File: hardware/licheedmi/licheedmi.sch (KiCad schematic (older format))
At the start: 17 parts

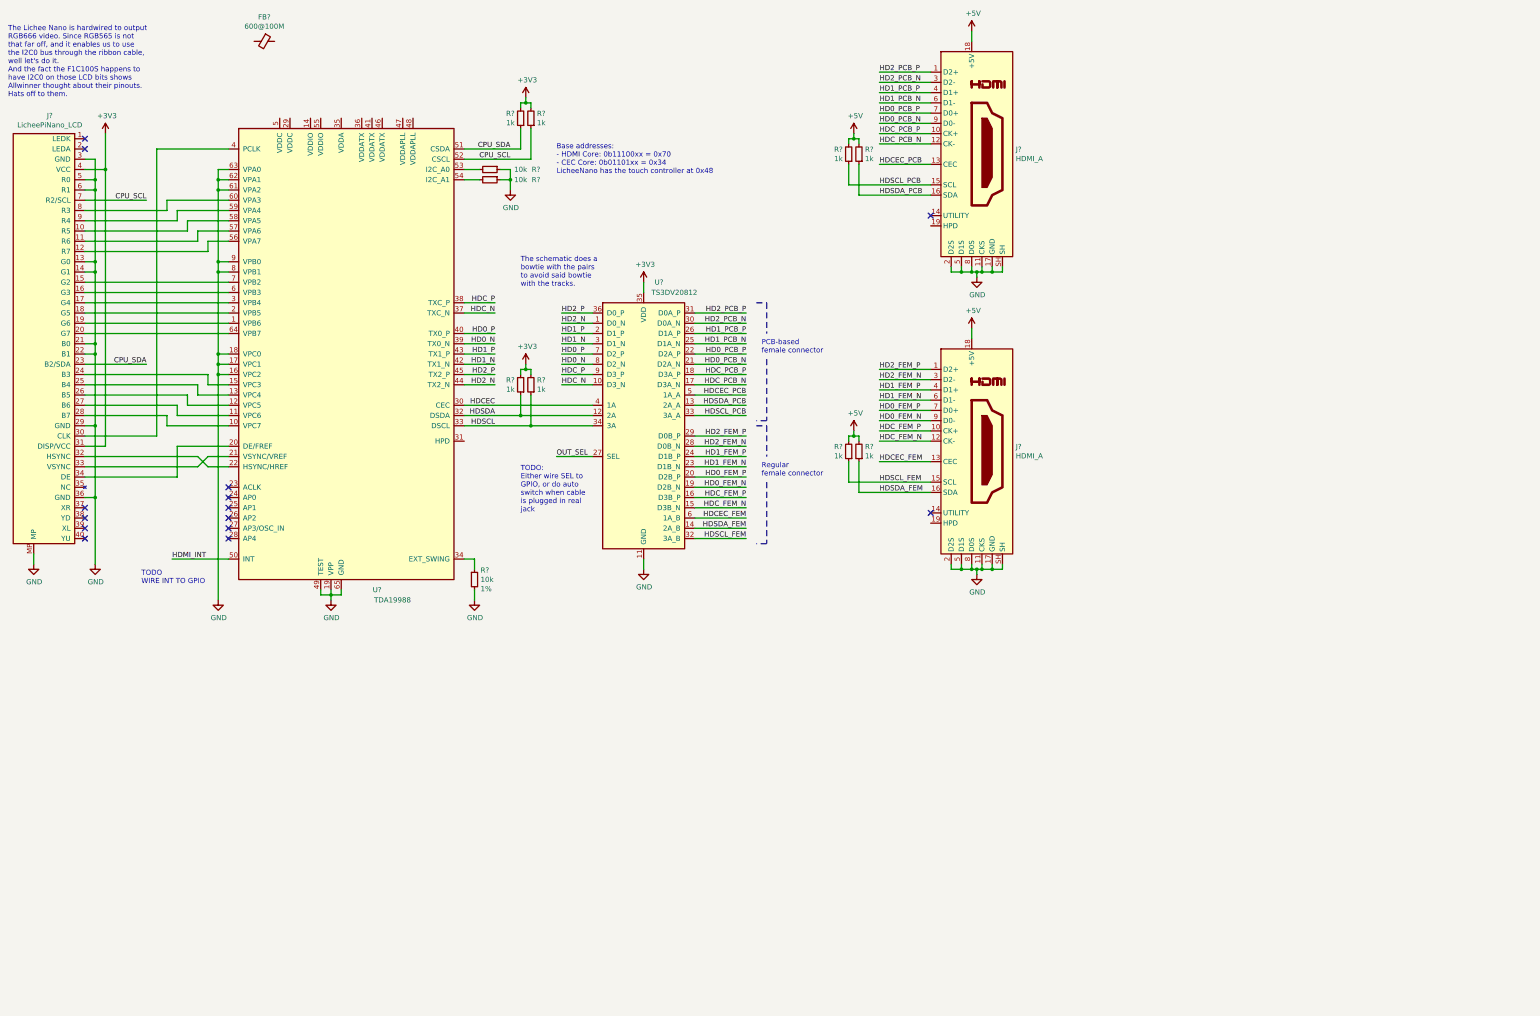
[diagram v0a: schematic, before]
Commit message: sch: Add HDMI 1.8V PSU
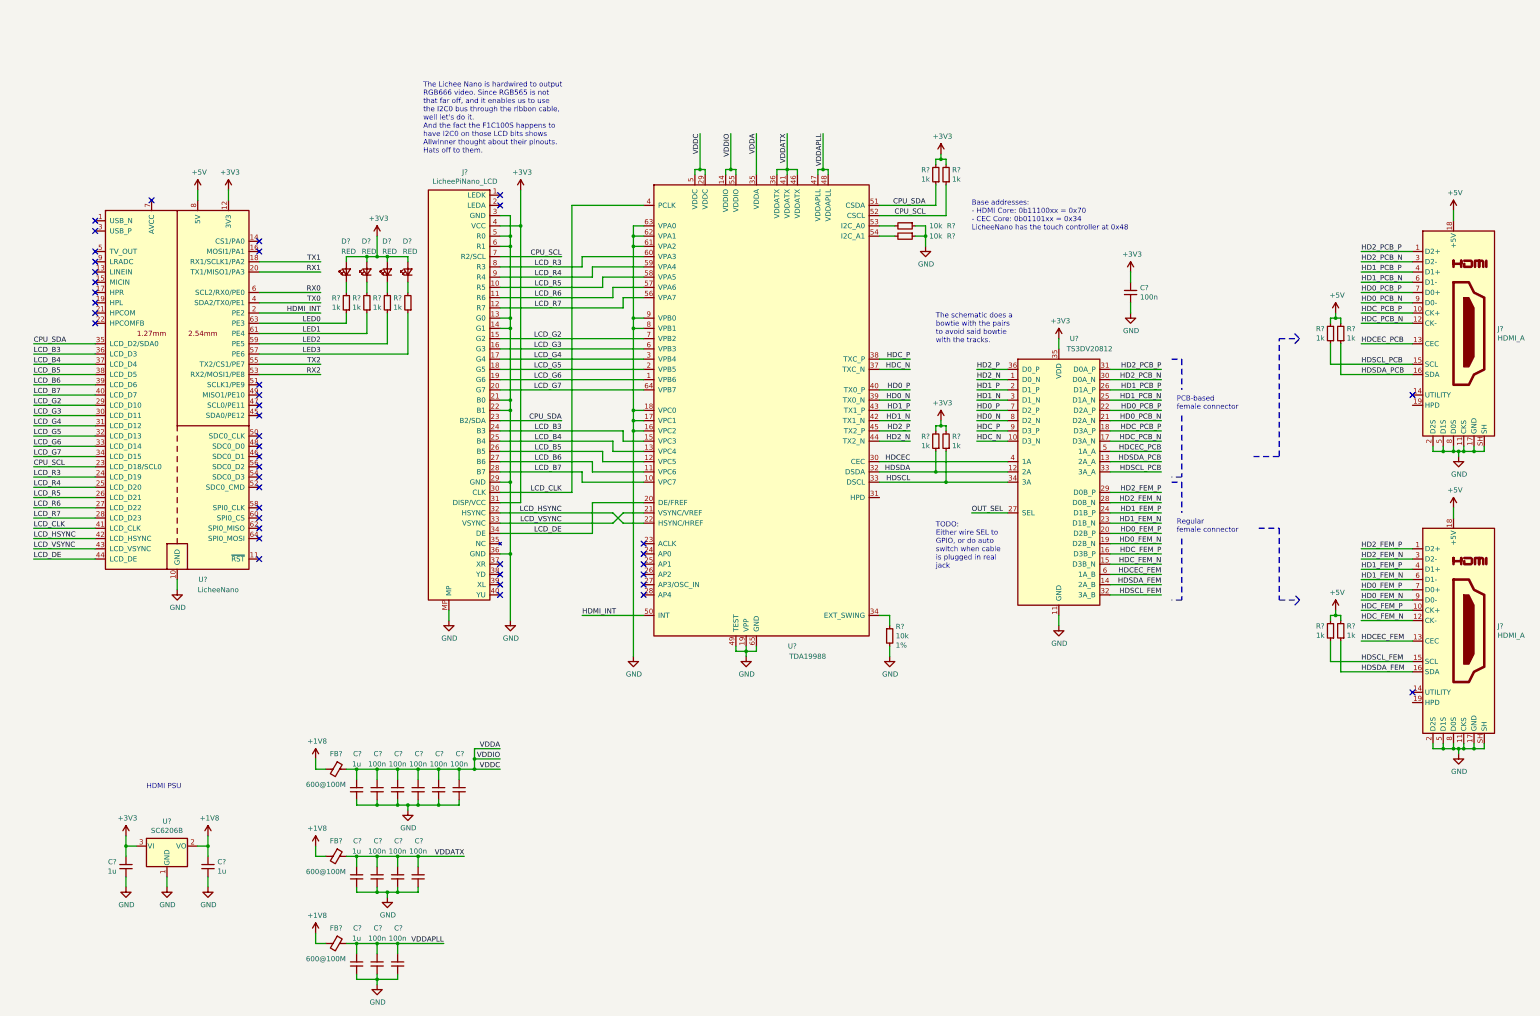
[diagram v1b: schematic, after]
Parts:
- added C? (x5): 1u, Capacitor_SMD:C_0603_1608Metric, symbol Device:C_Small
- added C? (x11): 100n, Capacitor_SMD:C_0603_1608Metric, symbol Device:C_Small
- added D? (x4): RED, symbol Device:LED_Small
- added FB? (x2): 600@100M, Inductor_SMD:L_0603_1608Metric, symbol Device:Ferrite_Bead_Small
- added R? (x4): 1k, Resistor_SMD:R_0603_1608Metric, symbol Device:R_Small
- added U?: LicheeNano, hdmizness:LicheeNano, symbol hdmizness:LicheeNano
- added U?: SC6206B, Package_TO_SOT_SMD:SOT-23, symbol hdmizness:SC6206B
- FB?: footprint (none) -> Inductor_SMD:L_0603_1608Metric
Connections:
- net +3V3: now also C?.1, C?.1, D?.2 (A), D?.2 (A), D?.2 (A), D?.2 (A), U?.12 (3V3), U?.3 (VI)
- net +5V: now also U?.8 (5V)
- net CPU_SCL: now also U?.23 (LCD_D18/SCL0)
- net CPU_SDA: now also U?.35 (LCD_D2/SDA0)
- net GND: now also C?.2, C?.2, C?.2, C?.2, C?.2, C?.2, C?.2, C?.2, C?.2, C?.2, C?.2, C?.2, C?.2, C?.2, C?.2, C?.2, U?.1 (GND), U?.10 (GND)
- net HDMI_INT: now also U?.2 (PE2)
- net LCD_G6: now reaches J?.19 (G6), U?.1 (VPB6)
- net LCD_G6: now also U?.33 (LCD_D14)
- net LCD_B7: now reaches J?.28 (B7), U?.10 (VPC7)
- net LCD_B7: now also U?.40 (LCD_D7)
- net LCD_B6: now reaches J?.27 (B6), U?.11 (VPC6)
- net LCD_B6: now also U?.39 (LCD_D6)
- net LCD_B5: now reaches J?.26 (B5), U?.12 (VPC5)
- net LCD_B5: now also U?.38 (LCD_D5)
- net LCD_B4: now reaches J?.25 (B4), U?.13 (VPC4)
- net LCD_B4: now also U?.37 (LCD_D4)
- net VDDA: now reaches U?.14 (VDDIO)
- net VDDA: now also U?.29 (VDDC), U?.35 (VDDA), U?.5 (VDDC), U?.55 (VDDIO), C?.1, C?.1, C?.1, C?.1, C?.1, C?.1, FB?.1
- net LCD_B3: now reaches J?.24 (B3), U?.15 (VPC3)
- net LCD_B3: now also U?.36 (LCD_D3)
- net LCD_G5: now reaches J?.18 (G5), U?.2 (VPB5)
- net LCD_G5: now also U?.32 (LCD_D13)
- net LCD_DE: now reaches J?.34 (DE), U?.20 (DE/FREF)
- net LCD_DE: now also U?.44 (LCD_DE)
- net LCD_VSYNC: now reaches J?.33 (VSYNC), U?.21 (VSYNC/VREF)
- net LCD_VSYNC: now also U?.43 (LCD_VSYNC)
- net LCD_HSYNC: now reaches J?.32 (HSYNC), U?.22 (HSYNC/HREF)
- net LCD_HSYNC: now also U?.42 (LCD_HSYNC)
- net LCD_G4: now reaches J?.17 (G4), U?.3 (VPB4)
- net LCD_G4: now also U?.31 (LCD_D12)
- net VDDATX: now reaches U?.36 (VDDATX)
- net VDDATX: now also FB?.1, U?.41 (VDDATX), U?.46 (VDDATX), C?.1, C?.1, C?.1, C?.1
- net LCD_CLK: now reaches J?.30 (CLK), U?.4 (PCLK)
- net LCD_CLK: now also U?.41 (LCD_CLK)
- net VDDAPLL: now reaches U?.47 (VDDAPLL)
- net VDDAPLL: now also U?.48 (VDDAPLL), C?.1, C?.1, C?.1, FB?.1
- net LCD_R7: now reaches J?.12 (R7), U?.56 (VPA7)
- net LCD_R7: now also U?.28 (LCD_D23)
- net LCD_R6: now reaches J?.11 (R6), U?.57 (VPA6)
- net LCD_R6: now also U?.27 (LCD_D22)
- net LCD_R5: now reaches J?.10 (R5), U?.58 (VPA5)
- net LCD_R5: now also U?.26 (LCD_D21)
- net LCD_R4: now reaches J?.9 (R4), U?.59 (VPA4)
- net LCD_R4: now also U?.25 (LCD_D20)
- net LCD_G3: now reaches J?.16 (G3), U?.6 (VPB3)
- net LCD_G3: now also U?.30 (LCD_D11)
- net LCD_R3: now reaches J?.8 (R3), U?.60 (VPA3)
- net LCD_R3: now also U?.24 (LCD_D19)
- net LCD_G7: now reaches J?.20 (G7), U?.64 (VPB7)
- net LCD_G7: now also U?.34 (LCD_D15)
- net LCD_G2: now reaches J?.15 (G2), U?.7 (VPB2)
- net LCD_G2: now also U?.29 (LCD_D10)
- net +1V8: now reaches FB?.2
- net +1V8: now also C?.1, FB?.2, FB?.2, U?.2 (VO)
- new net: D?.1 (K), R?.2 (x4)
- new net LED0: R?.1, U?.63 (PE3)
- new net LED1: R?.1, U?.61 (PE4)
- new net LED2: R?.1, U?.59 (PE5)
- new net LED3: R?.1, U?.57 (PE6)
- new net RX0: U?.6 (SCL2/RX0/PE0)
- new net RX1: U?.20 (TX1/MISO1/PA3)
- new net RX2: U?.53 (RX2/MOSI1/PE8)
- new net TX0: U?.4 (SDA2/TX0/PE1)
- new net TX1: U?.18 (RX1/SCLK1/PA2)
- new net TX2: U?.55 (TX2/CS1/PE7)
- no-connect marks 14 -> 42
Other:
- note added: "HDMI PSU"
- note removed: "TODO\nWIRE INT TO GPIO"
- moved on the sheet: FB?, J?, R?, U?

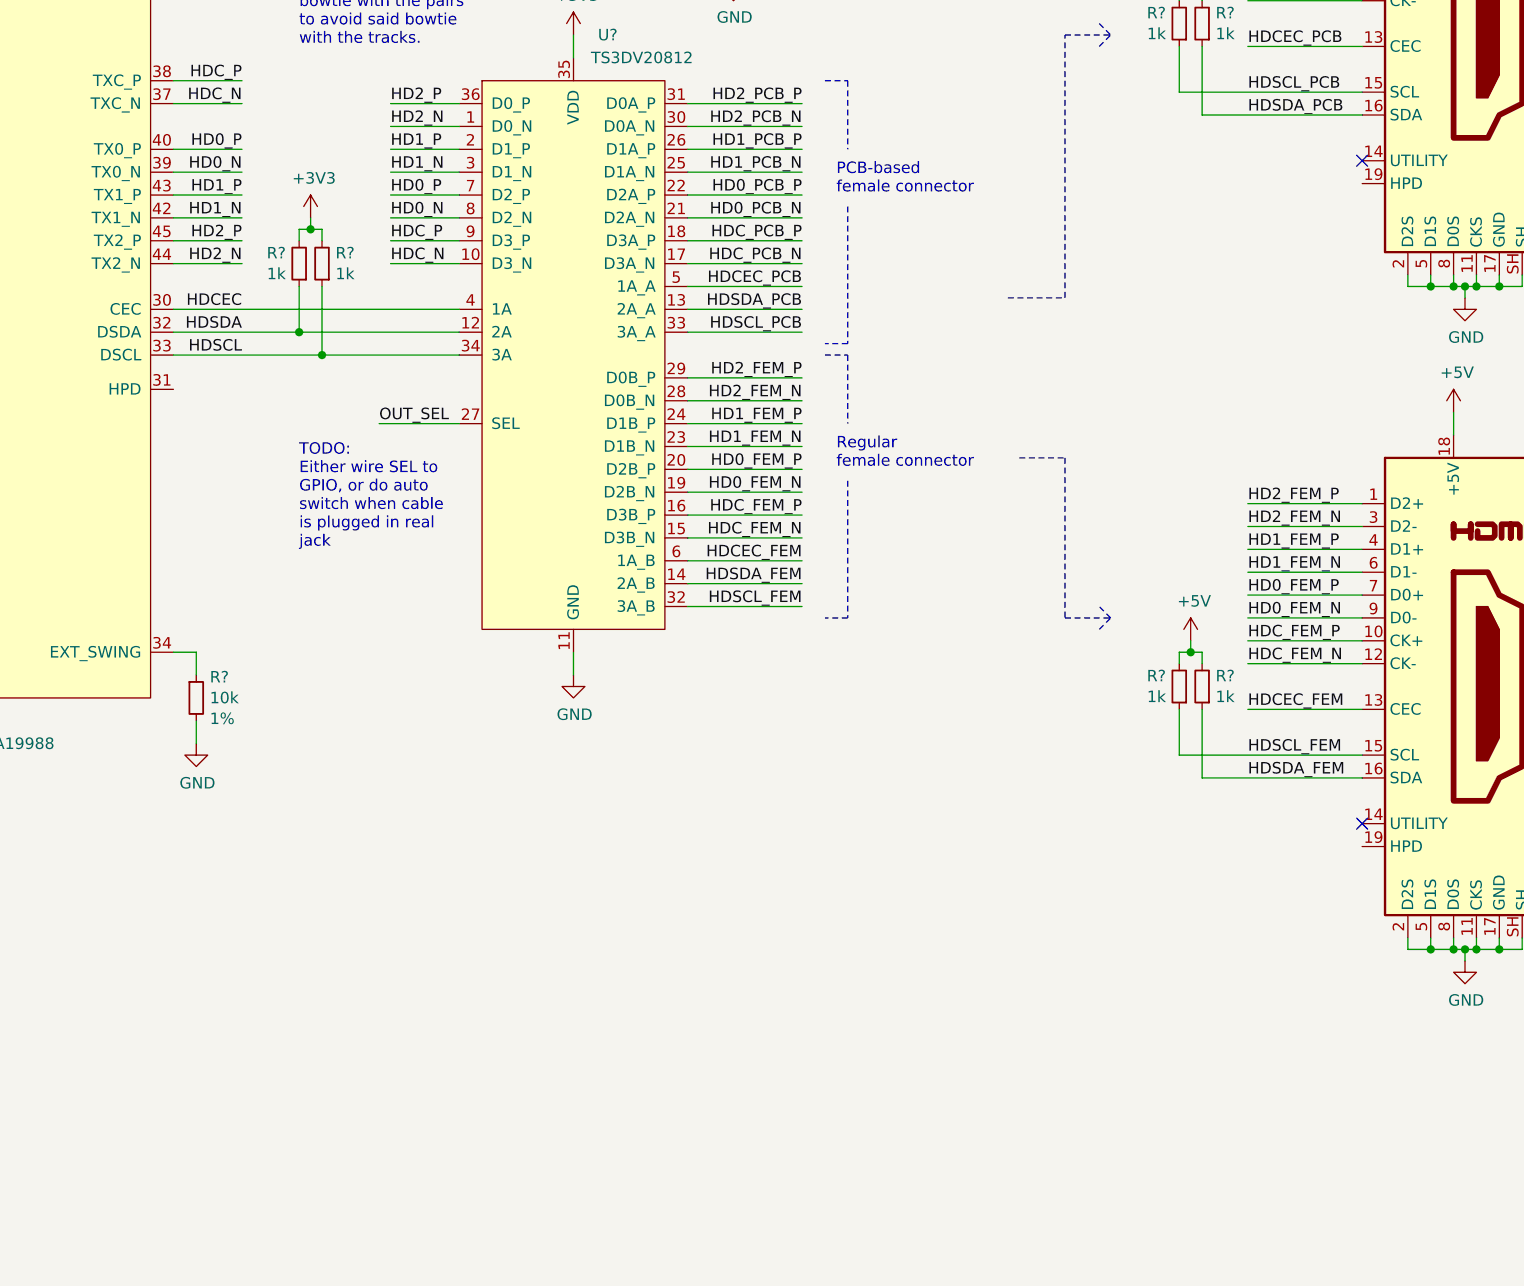
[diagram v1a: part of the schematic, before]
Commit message: sch: Add HPD handling
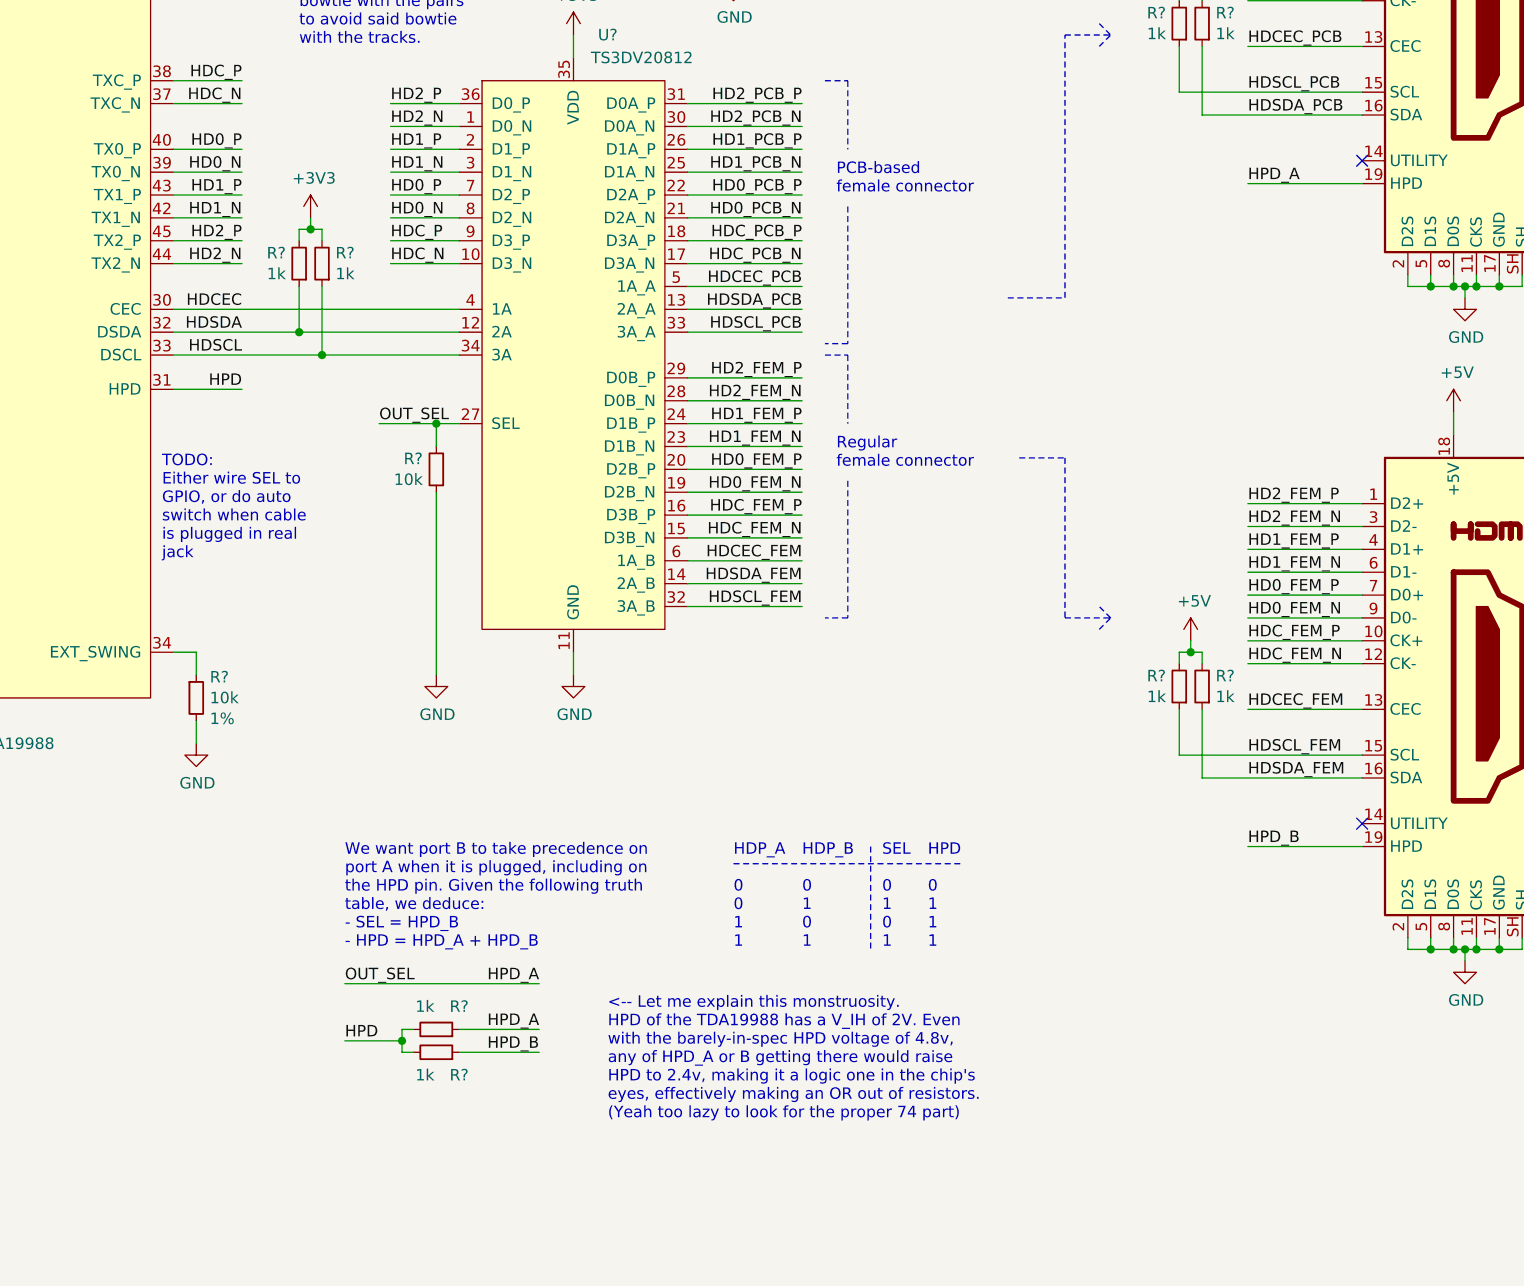
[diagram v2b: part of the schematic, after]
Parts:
- added R?: 10k, Resistor_SMD:R_0603_1608Metric, symbol Device:R_Small
- added R? (x2): 1k, Resistor_SMD:R_0603_1608Metric, symbol Device:R_Small
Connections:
- net OUT_SEL is gone; now on net HPD_A: U?.27 (SEL)
- net GND: now also R?.1
- net HPD: now reaches U?.31 (HPD)
- net HPD: now also R?.2, R?.2
- net HPD_A: now reaches J?.19 (HPD)
- net HPD_A: now also R?.1, R?.2
- net HPD_B: now reaches J?.19 (HPD)
- net HPD_B: now also R?.1
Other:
- note added: "<-- Let me explain this monstruosity.\nHPD of the TDA19988 has a V_IH of 2V. Even\nwith the barely-in-spec HPD voltage of 4.8v,\nany of HPD_A or B getting there would raise\nHPD to 2.4v, making it a logic one in the chip's\neyes, effectively making an OR out of resistors.\n(Yeah too lazy to look for the proper 74 part)"
- note added: "HDP_A\n\n0\n0\n1\n1"
- note added: "HDP_B\n\n0\n1\n0\n1"
- note added: "HPD\n\n0\n1\n1\n1"
- note added: "SEL\n\n0\n1\n0\n1"
- note added: "We want port B to take precedence on\nport A when it is plugged, including on\nthe HPD pin. Given the following truth\ntable, we deduce:\n- SEL = HPD_B\n- HPD = HPD_A + HPD_B"
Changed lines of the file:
@@
 $EndComp
 Wire Wire Line
-	10550 5550 10200 5550
-Text Label 10200 5550 0    50   ~ 0
-OUT_SEL
-Text Notes 9850 6100 0    50   ~ 0
+	10550 5550 10450 5550
+Text Notes 9250 6150 0    50   ~ 0
 TODO:\nEither wire SEL to\nGPIO, or do auto\nswitch when cable\nis plugged in real\njack
 Wire Wire Line
@@
 Wire Notes Line
 	13400 6400 13350 6350
+$Comp
+L Device:R_Small R?
+U 1 1 60F47BFD
+P 10450 5750
+F 0 "R?" H 10509 5704 50  0000 L CNN
+F 1 "10k" H 10509 5795 50  0000 L CNN
+F 2 "Resistor_SMD:R_0603_1608Metric" H 10450 5750 50  0001 C CNN
+F 3 "~" H 10450 5750 50  0001 C CNN
+	1    10450 5750
+	-1   0    0    1
+$EndComp
+Wire Wire Line
+	10450 5650 10450 5550
+$Comp
+L power:GND #PWR?
+U 1 1 60F76D01
+P 10450 6650
+F 0 "#PWR?" H 10450 6400 50  0001 C CNN
+F 1 "GND" H 10455 6477 50  0000 C CNN
+F 2 "" H 10450 6650 50  0001 C CNN
+F 3 "" H 10450 6650 50  0001 C CNN
+	1    10450 6650
+	1    0    0    -1
+$EndComp
+Wire Wire Line
+	10450 6650 10450 5850
+Text Notes 10050 7850 0    50   ~ 0
+We want port B to take precedence on\nport A when it is plugged, including on\nthe HPD pin. Given the following truth\ntable, we deduce:\n- SEL = HPD_B\n- HPD = HPD_A + HPD_B
+Text Notes 11750 7850 0    50   ~ 0
+HDP_A\n\n0\n0\n1\n1
+Text Notes 12050 7850 0    50   ~ 0
+HDP_B\n\n0\n1\n0\n1
+Text Notes 12400 7850 0    50   ~ 0
+SEL\n\n0\n1\n0\n1
+Text Notes 12600 7850 0    50   ~ 0
+HPD\n\n0\n1\n1\n1
+Wire Notes Line
+	11750 7475 12750 7475
+Wire Notes Line
+	12350 7400 12350 7850
+Text Label 14000 7400 0    50   ~ 0
+HPD_B
+Wire Wire Line
+	14000 7400 14500 7400
+Text Label 14000 4500 0    50   ~ 0
+HPD_A
+Wire Wire Line
+	14000 4500 14500 4500
+Text Label 10900 8000 2    50   ~ 0
+HPD_A
+Connection ~ 10450 5550
+Wire Wire Line
+	10450 5550 10200 5550
+Text Label 10200 5550 0    50   ~ 0
+OUT_SEL
+Text Label 10050 8000 0    50   ~ 0
+OUT_SEL
+Wire Wire Line
+	10050 8000 10900 8000
+$Comp
+L Device:R_Small R?
+U 1 1 61201D62
+P 10450 8200
+F 0 "R?" V 10550 8300 50  0000 C CNN
+F 1 "1k" V 10550 8150 50  0000 C CNN
+F 2 "Resistor_SMD:R_0603_1608Metric" H 10450 8200 50  0001 C CNN
+F 3 "~" H 10450 8200 50  0001 C CNN
+	1    10450 8200
+	0    1    -1   0
+$EndComp
+$Comp
+L Device:R_Small R?
+U 1 1 61201D68
+P 10450 8300
+F 0 "R?" V 10350 8400 50  0000 C CNN
+F 1 "1k" V 10350 8250 50  0000 C CNN
+F 2 "Resistor_SMD:R_0603_1608Metric" H 10450 8300 50  0001 C CNN
+F 3 "~" H 10450 8300 50  0001 C CNN
+	1    10450 8300
+	0    1    -1   0
+$EndComp
+Wire Wire Line
+	10350 8200 10300 8200
+Wire Wire Line
+	10300 8200 10300 8250
+Wire Wire Line
+	10300 8300 10350 8300
+Connection ~ 10300 8250
+Wire Wire Line
+	10300 8250 10300 8300
+Wire Wire Line
+	10550 8200 10900 8200
+Wire Wire Line
+	10900 8300 10550 8300
+Wire Wire Line
+	10300 8250 10050 8250
+Text Label 10900 8200 2    50   ~ 0
+HPD_A
+Text Label 10900 8300 2    50   ~ 0
+HPD_B
+Wire Wire Line
+	9300 5400 9600 5400
+Text Label 9600 5400 2    50   ~ 0
+HPD
+Text Label 10050 8250 0    50   ~ 0
+HPD
+Text Notes 11200 8600 0    50   ~ 0
+<-- Let me explain this monstruosity.\nHPD of the TDA19988 has a V_IH of 2V. Even\nwith the barely-in-spec HPD voltage of 4.8v,\nany of HPD_A or B getting there would raise\nHPD to 2.4v, making it a logic one in the chip's\neyes, effectively making an OR out of resistors.\n(Yeah too lazy to look for the proper 74 part)
 $EndSCHEMATC
